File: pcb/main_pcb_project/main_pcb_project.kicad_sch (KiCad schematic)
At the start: 0 parts

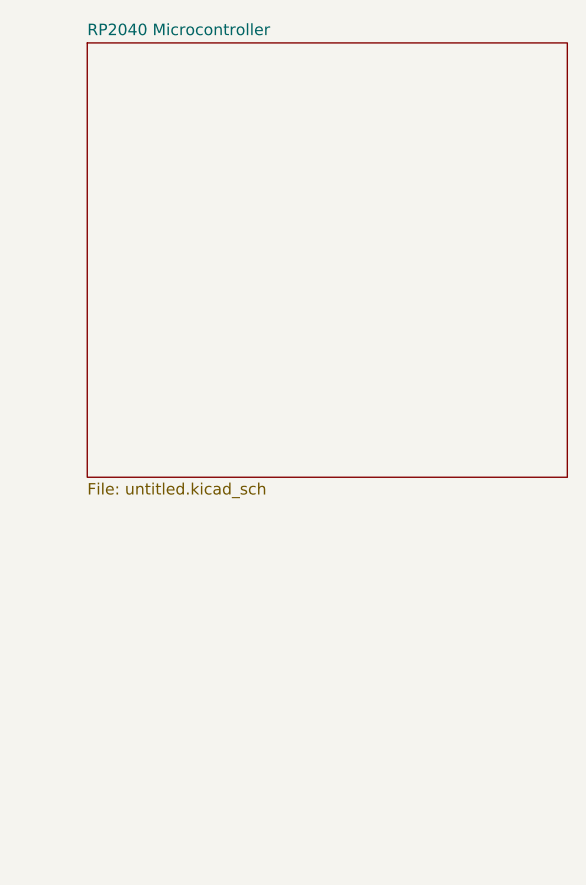
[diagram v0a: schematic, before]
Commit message: Continued RP2040 implementation
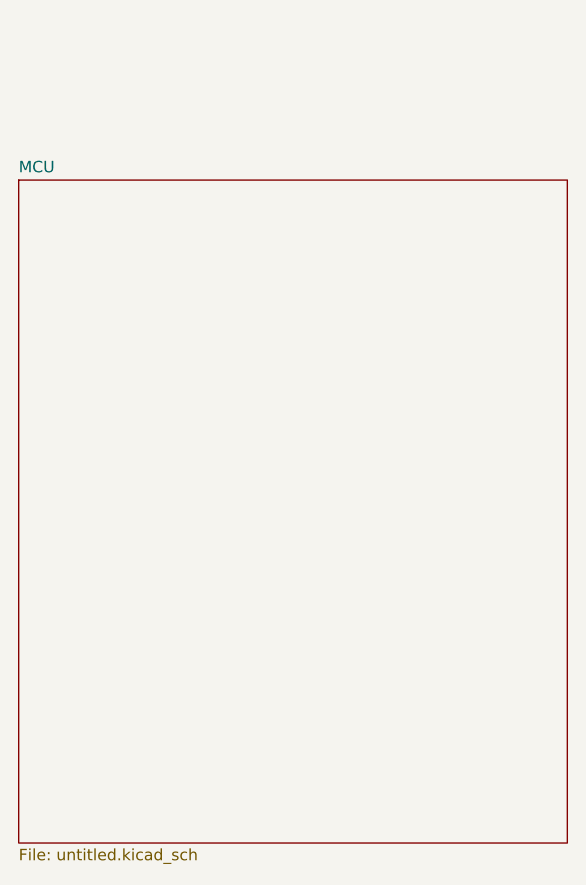
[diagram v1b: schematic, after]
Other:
- sheet RP2040 Microcontroller renamed MCU
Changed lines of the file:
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@@
 	)
 	(sheet
-		(at 118.11 26.67)
-		(size 53.34 48.26)
+		(at 110.49 41.91)
+		(size 60.96 73.66)
 		(exclude_from_sim no)
 		(in_bom yes)
@@
 			(color 0 0 0 0)
 		)
-		(property "Sheetname" "RP2040 Microcontroller"
-			(at 118.11 25.9584 0)
+		(property "Sheetname" "MCU"
+			(at 110.49 41.1984 0)
 			(show_name no)
 			(do_not_autoplace no)
@@
 		)
 		(property "Sheetfile" "untitled.kicad_sch"
-			(at 118.11 75.5146 0)
+			(at 110.49 116.1546 0)
 			(show_name no)
 			(do_not_autoplace no)
